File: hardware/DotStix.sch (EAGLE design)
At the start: 23 parts, among them IC1 CAT24M010TS, Q2 BSH103, U1 ATMEGA328P-MU-QFN32, U2 TMP102

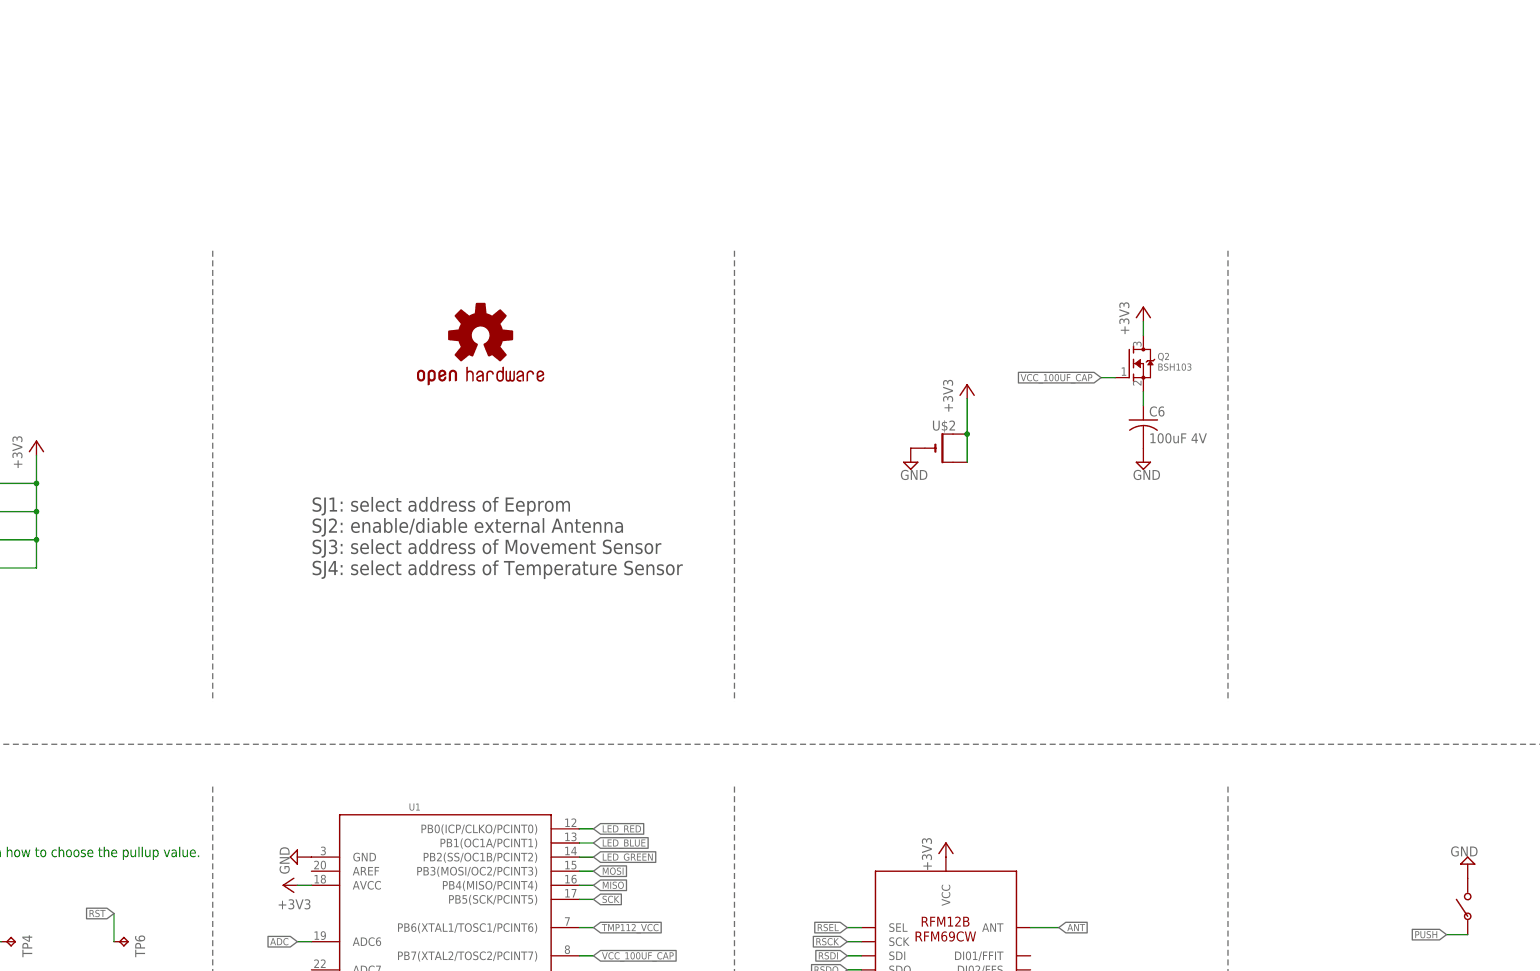
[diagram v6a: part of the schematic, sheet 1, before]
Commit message: Remove NMOSFET, connect 100uF to IO directly
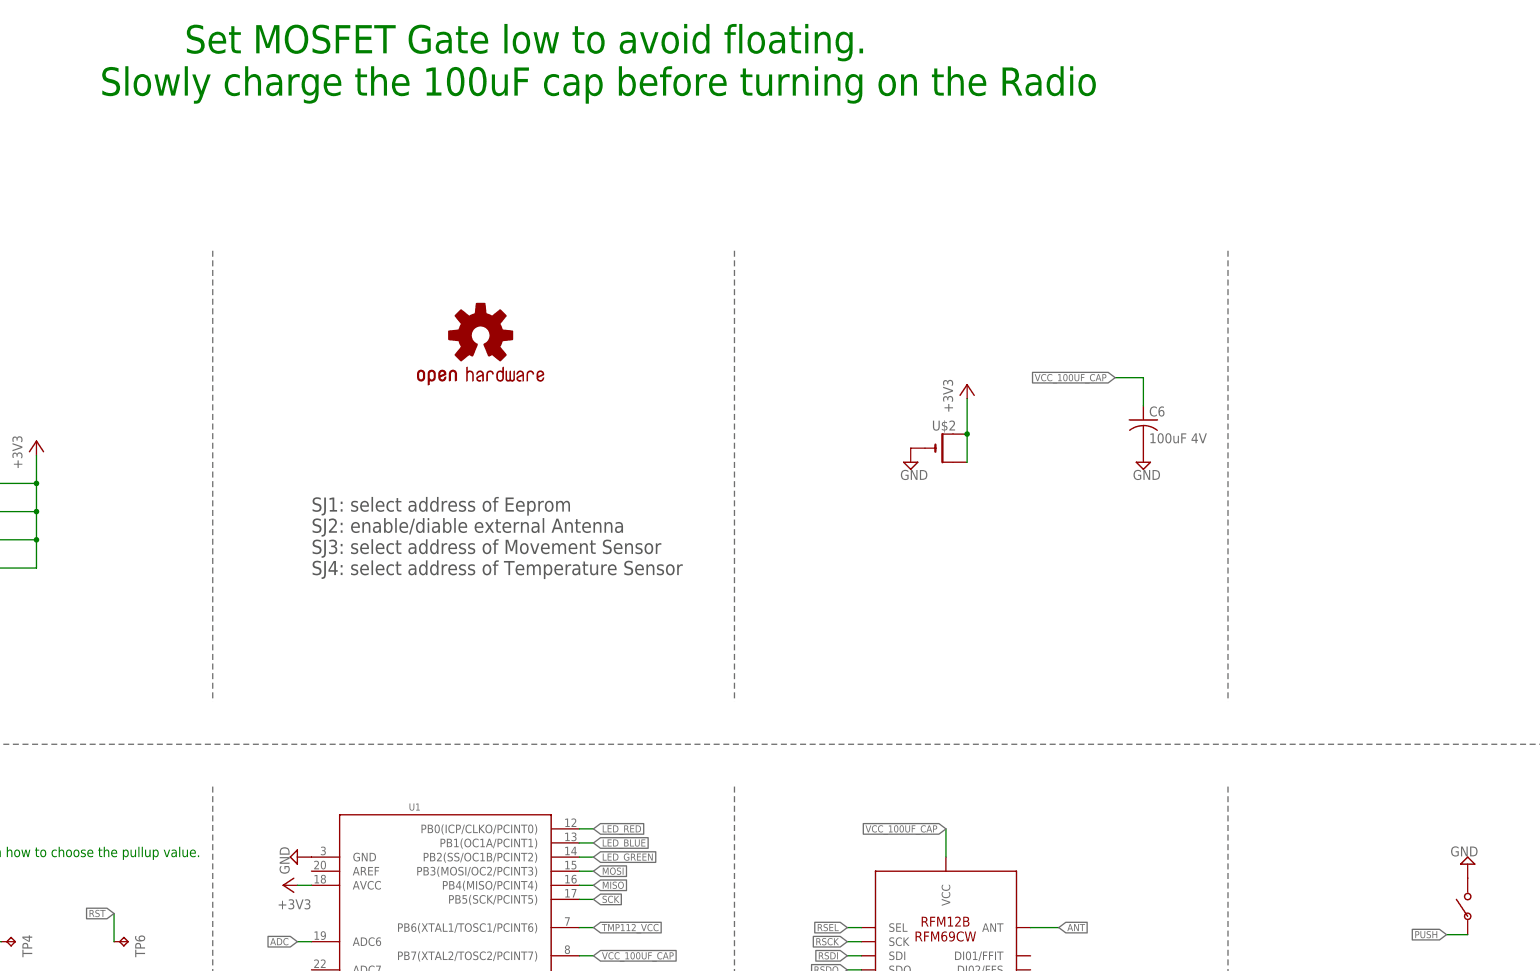
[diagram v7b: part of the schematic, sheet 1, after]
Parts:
- removed Q2: BSH103, adafruit:MOSFET-NREFLOW
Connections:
- removed net N$5: C6.1, Q2.S
- net +3V3: no longer Q2.D, U$1.VCC
- net VCC_100UF_CAP: now also C6.1, U$1.VCC; no longer Q2.G
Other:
- note added: "Set MOSFET Gate low to avoid floating."
- note added: "Slowly charge the 100uF cap before turning on the Radio"
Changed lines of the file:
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@@
 <setting verticaltext="up"/>
 </settings>
-<grid distance="0.05" unitdist="inch" unit="inch" style="lines" multiple="1" display="no" altdistance="0.01" altunitdist="inch" altunit="inch"/>
+<grid distance="0.1" unitdist="inch" unit="inch" style="lines" multiple="1" display="no" altdistance="0.01" altunitdist="inch" altunit="inch"/>
 <layers>
 <layer number="1" name="Top" color="4" fill="1" visible="no" active="no"/>
@@
 <part name="U$1" library="rfm12b_withoutPlanes" deviceset="RFM12B/69CW" device=""/>
 <part name="+3V4" library="supply1" deviceset="+3V3" device=""/>
-<part name="+3V5" library="supply1" deviceset="+3V3" device=""/>
 <part name="LOGO1" library="Particle-Devices" deviceset="OSHW-LOGO" device="S"/>
 <part name="+3V2" library="supply1" deviceset="+3V3" device=""/>
@@
 <part name="R5" library="resistor" deviceset="R-EU_" device="R0603" value="470kΩ"/>
 <part name="+3V8" library="supply1" deviceset="+3V3" device=""/>
-<part name="+3V10" library="supply1" deviceset="+3V3" device=""/>
 <part name="SUPPLY16" library="supply2" deviceset="GND" device=""/>
 <part name="C6" library="adafruit" deviceset="C-US" device="C3216" value="100uF 4V"/>
@@
 <part name="TP5" library="testpad" deviceset="TP" device="TP20SQ"/>
 <part name="TP6" library="testpad" deviceset="TP" device="TP20SQ"/>
-<part name="Q2" library="adafruit" deviceset="MOSFET-N" device="REFLOW" value="BSH103"/>
 <part name="U$4" library="pusbbutton_4x2_5" deviceset="PUSHBUTTON_4X2.5" device=""/>
 <part name="SUPPLY8" library="supply2" deviceset="GND" device=""/>
@@
 <text x="167.64" y="-81.28" size="3.81" layer="95">Storage</text>
 <text x="386.08" y="173.99" size="1.27" layer="91">TMP112 needs VCC from MCU I/O. (reduces draw from 7uA -&gt; ? nA)</text>
+<text x="124.46" y="226.06" size="5.08" layer="91">Set MOSFET Gate low to avoid floating.</text>
+<text x="109.22" y="218.44" size="5.08" layer="91">Slowly charge the 100uF cap before turning on the Radio</text>
 </plain>
 <instances>
@@
 <instance part="U$1" gate="G$1" x="261.62" y="58.42"/>
 <instance part="+3V4" gate="G$1" x="147.32" y="55.88"/>
-<instance part="+3V5" gate="G$1" x="261.62" y="83.82"/>
 <instance part="LOGO1" gate="G$1" x="177.8" y="175.26"/>
 <instance part="+3V2" gate="G$1" x="142.24" y="76.2" rot="R90"/>
@@
 <instance part="R5" gate="G$1" x="78.74" y="71.12" rot="R90"/>
 <instance part="+3V8" gate="G$1" x="78.74" y="78.74"/>
-<instance part="+3V10" gate="G$1" x="297.18" y="180.34"/>
 <instance part="SUPPLY16" gate="GND" x="297.18" y="152.4"/>
 <instance part="C6" gate="G$1" x="297.18" y="160.02"/>
@@
 <instance part="TP5" gate="G$1" x="114.3" y="55.88" rot="R270"/>
 <instance part="TP6" gate="G$1" x="114.3" y="66.04" rot="R270"/>
-<instance part="Q2" gate="G$1" x="294.64" y="170.18"/>
 <instance part="U$4" gate="G$1" x="355.6" y="72.39" rot="R90"/>
 <instance part="SUPPLY8" gate="GND" x="355.6" y="80.01" rot="R180"/>
@@
 <pinref part="+3V4" gate="G$1" pin="+3V3"/>
 <junction x="147.32" y="53.34"/>
-</segment>
-<segment>
-<pinref part="U$1" gate="G$1" pin="VCC"/>
-<pinref part="+3V5" gate="G$1" pin="+3V3"/>
 </segment>
 <segment>
@@
 <pinref part="+3V14" gate="G$1" pin="+3V3"/>
 </segment>
-<segment>
-<pinref part="+3V10" gate="G$1" pin="+3V3"/>
-<pinref part="Q2" gate="G$1" pin="D"/>
-<wire x1="297.18" y1="177.8" x2="297.18" y2="175.26" width="0.1524" layer="91"/>
-</segment>
 </net>
 <net name="MOSI" class="0">
@@
 </segment>
 </net>
-<net name="N$5" class="0">
-<segment>
-<pinref part="C6" gate="G$1" pin="1"/>
-<pinref part="Q2" gate="G$1" pin="S"/>
-<wire x1="297.18" y1="165.1" x2="297.18" y2="162.56" width="0.1524" layer="91"/>
-</segment>
-</net>
 <net name="VCC_100UF_CAP" class="0">
-<segment>
-<pinref part="Q2" gate="G$1" pin="G"/>
-<wire x1="292.1" y1="167.64" x2="289.56" y2="167.64" width="0.1524" layer="91"/>
-<label x="289.56" y="167.64" size="1.27" layer="95" rot="R180" xref="yes"/>
-</segment>
 <segment>
 <pinref part="U1" gate="G$1" pin="PB7(XTAL2/TOSC2/PCINT7)"/>
@@
 <label x="198.12" y="63.5" size="1.27" layer="95" xref="yes"/>
 </segment>
-</net>
+<segment>
+<pinref part="C6" gate="G$1" pin="1"/>
+<wire x1="297.18" y1="162.56" x2="297.18" y2="167.64" width="0.1524" layer="91"/>
+<wire x1="297.18" y1="167.64" x2="292.1" y2="167.64" width="0.1524" layer="91"/>
+<label x="292.1" y="167.64" size="1.27" layer="95" rot="R180" xref="yes"/>
+</segment>
+<segment>
+<pinref part="U$1" gate="G$1" pin="VCC"/>
+<wire x1="261.62" y1="81.28" x2="261.62" y2="86.36" width="0.1524" layer="91"/>
+<label x="261.62" y="86.36" size="1.27" layer="95" rot="R180" xref="yes"/>
+</segment>
+</net>

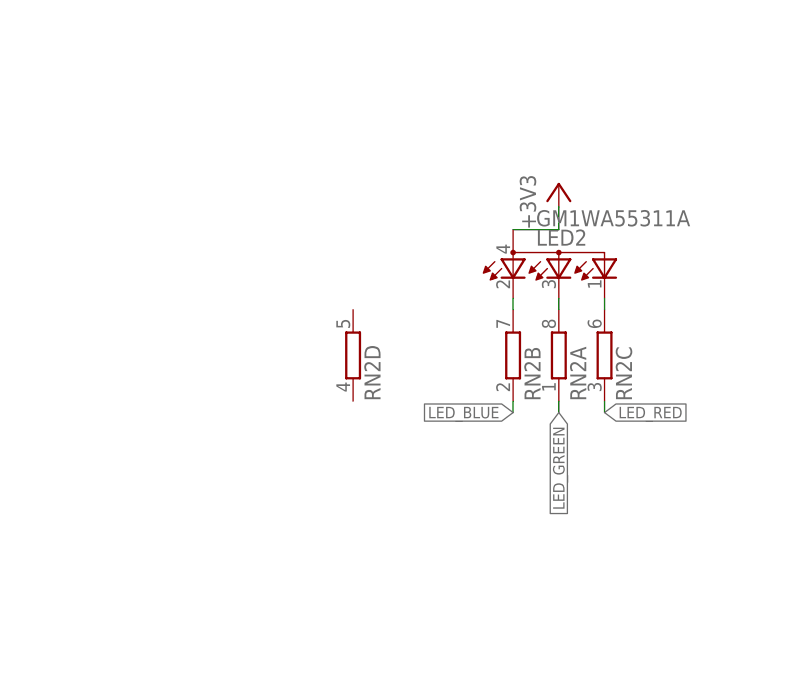
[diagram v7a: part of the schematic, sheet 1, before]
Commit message: Led on INT_MULTIPLE, tStop for Supercap GND
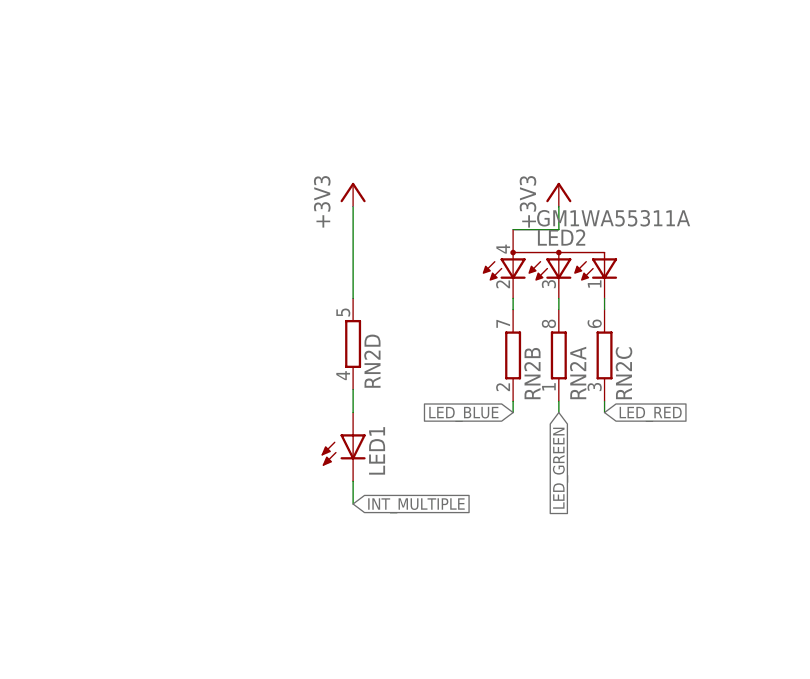
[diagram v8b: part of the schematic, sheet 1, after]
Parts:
- added LED1: (no value), led:LEDCHIP-LED0603
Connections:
- new net N$5: LED1.A, RN2D.1
- net +3V3: now also RN2D.2
- net INT_MULTIPLE: now also LED1.C
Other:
- moved on the sheet: RN2D
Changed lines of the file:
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@@
 <?xml version="1.0" encoding="utf-8"?>
 <!DOCTYPE eagle SYSTEM "eagle.dtd">
-<eagle version="7.7.0">
+<eagle version="9.1.0">
 <drawing>
 <settings>
 <setting alwaysvectorfont="no"/>
+<setting keepoldvectorfont="yes"/>
 <setting verticaltext="up"/>
 </settings>
@@
 <part name="U$4" library="pusbbutton_4x2_5" deviceset="PUSHBUTTON_4X2.5" device=""/>
 <part name="SUPPLY8" library="supply2" deviceset="GND" device=""/>
+<part name="+3V5" library="supply1" deviceset="+3V3" device=""/>
+<part name="LED1" library="led" library_urn="urn:adsk.eagle:library:259" deviceset="LED" device="CHIP-LED0603" package3d_urn="urn:adsk.eagle:package:15819/3"/>
 </parts>
 <sheets>
@@
 <instance part="RN2" gate="B" x="7.62" y="140.97" rot="R90"/>
 <instance part="RN2" gate="C" x="17.78" y="140.97" rot="R90"/>
-<instance part="RN2" gate="D" x="-10.16" y="140.97" rot="R90"/>
+<instance part="RN2" gate="D" x="-10.16" y="142.24" rot="R90"/>
 <instance part="U2" gate="G$1" x="407.67" y="160.02"/>
 <instance part="SUPPLY15" gate="GND" x="394.97" y="151.13"/>
@@
 <instance part="U$4" gate="G$1" x="355.6" y="72.39" rot="R90"/>
 <instance part="SUPPLY8" gate="GND" x="355.6" y="80.01" rot="R180"/>
+<instance part="+3V5" gate="G$1" x="-10.16" y="160.02"/>
+<instance part="LED1" gate="G$1" x="-10.16" y="132.08"/>
 </instances>
 <busses>
@@
 <pinref part="+3V14" gate="G$1" pin="+3V3"/>
 </segment>
+<segment>
+<pinref part="+3V5" gate="G$1" pin="+3V3"/>
+<pinref part="RN2" gate="D" pin="2"/>
+<wire x1="-10.16" y1="157.48" x2="-10.16" y2="147.32" width="0.1524" layer="91"/>
+</segment>
 </net>
 <net name="MOSI" class="0">
@@
 <label x="66.04" y="133.35" size="1.27" layer="95" rot="R180" xref="yes"/>
 </segment>
+<segment>
+<pinref part="LED1" gate="G$1" pin="C"/>
+<wire x1="-10.16" y1="127" x2="-10.16" y2="124.46" width="0.1524" layer="91"/>
+<label x="-10.16" y="124.46" size="1.27" layer="95" xref="yes"/>
+</segment>
 </net>
 <net name="N$2" class="0">
@@
 <wire x1="355.6" y1="67.31" x2="351.79" y2="67.31" width="0.1524" layer="91"/>
 <label x="351.79" y="67.31" size="1.27" layer="95" rot="R180" xref="yes"/>
+</segment>
+</net>
+<net name="N$5" class="0">
+<segment>
+<pinref part="RN2" gate="D" pin="1"/>
+<pinref part="LED1" gate="G$1" pin="A"/>
+<wire x1="-10.16" y1="137.16" x2="-10.16" y2="134.62" width="0.1524" layer="91"/>
 </segment>
 </net>
@@
 which will not be processed correctly with this version.
 </note>
+<note version="8.2" severity="warning">
+Since Version 8.2, EAGLE supports online libraries. The ids
+of those online libraries will not be understood (or retained)
+with this version.
+</note>
+<note version="8.3" severity="warning">
+Since Version 8.3, EAGLE supports URNs for individual library
+assets (packages, symbols, and devices). The URNs of those assets
+will not be understood (or retained) with this version.
+</note>
+<note version="8.3" severity="warning">
+Since Version 8.3, EAGLE supports the association of 3D packages
+with devices in libraries, schematics, and board files. Those 3D
+packages will not be understood (or retained) with this version.
+</note>
 </compatibility>
